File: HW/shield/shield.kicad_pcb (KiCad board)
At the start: 2 copper layers, 76.7 x 57 mm, 82 parts, among them J1 TRG, J2 E-STOP, J3 UART, J4 IO, J5 LDP-C BOB, J6 VIN, J7 BREAK, Q1 BSS138, Q2 BSS138, Q3 BSS138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

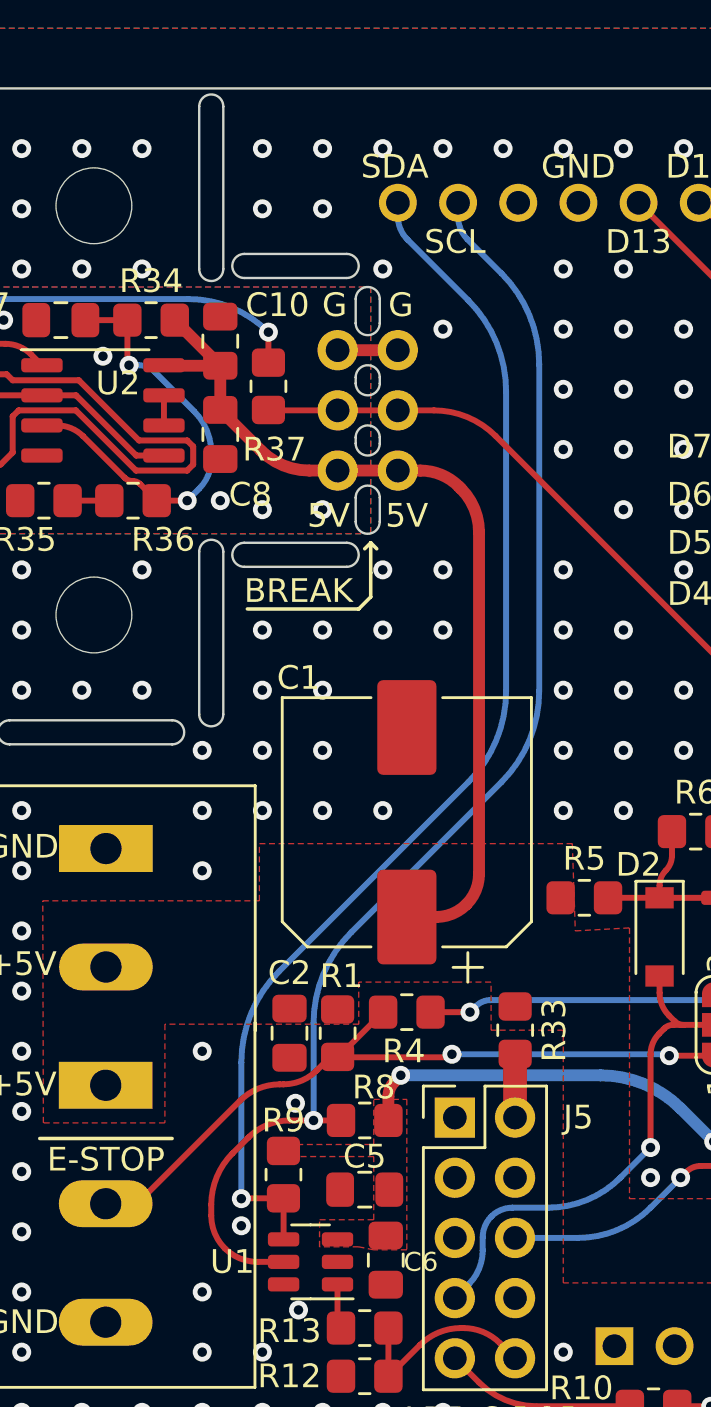
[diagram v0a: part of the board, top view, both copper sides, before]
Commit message: fixed flipped I2C lines in the board files
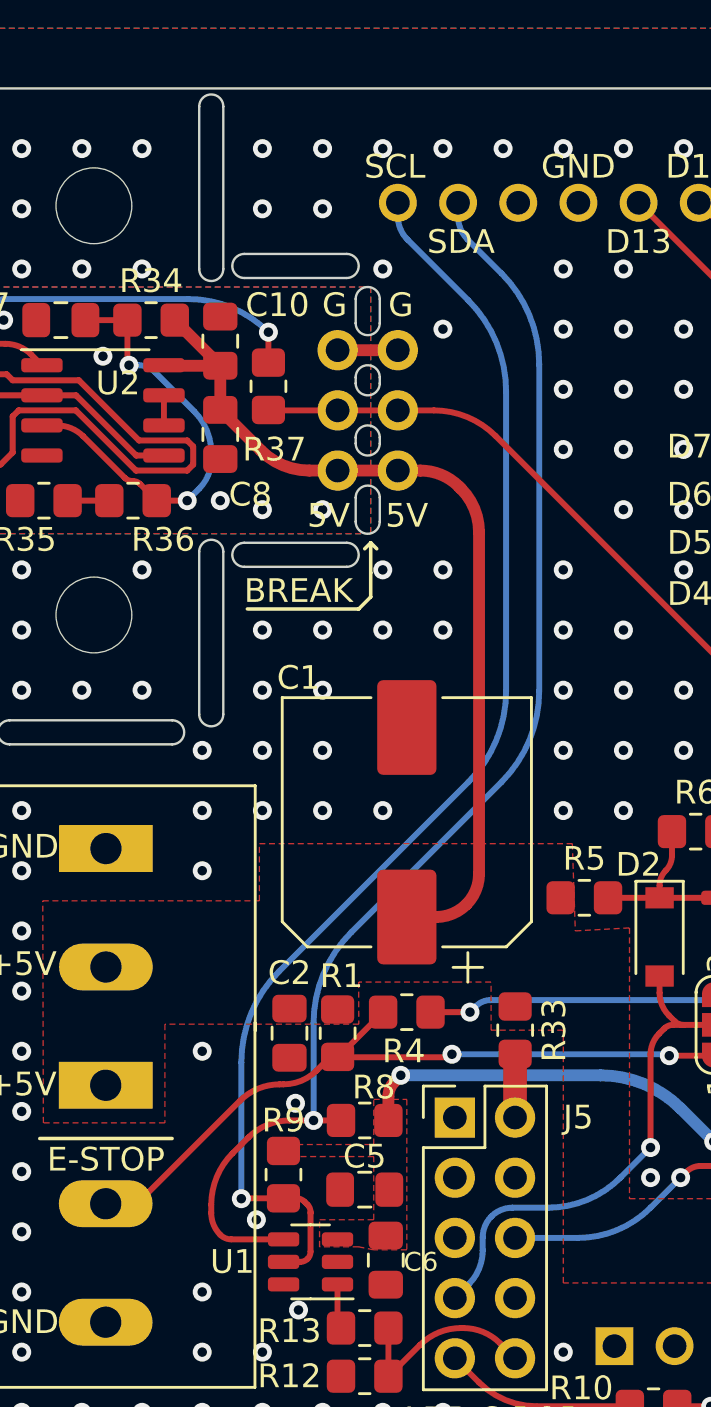
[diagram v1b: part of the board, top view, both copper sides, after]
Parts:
- C9: value 10p -> 3p
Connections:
- A1 pad 31: /SCL -> /SDA
- A1 pad 32: /SDA -> /SCL
- R8 pad 2: /SCL -> /SDA
- R9 pad 2: /SDA -> /SCL
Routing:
- net /SDA: track 51.2 -> 54.8 mm
- net /SCL: track 55.3 -> 54.0 mm
